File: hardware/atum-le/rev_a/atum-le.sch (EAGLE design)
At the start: 41 parts, among them J2 SH_MALE_2/1MM, J3 ATUM-HEADER, U1 CC2538, U2 FM25LBTDFN-8, U3 RV-3049-C3, U4 TPS62740, X1 EPSON-FA-128, X2 ABS05-32.768KHZ-T

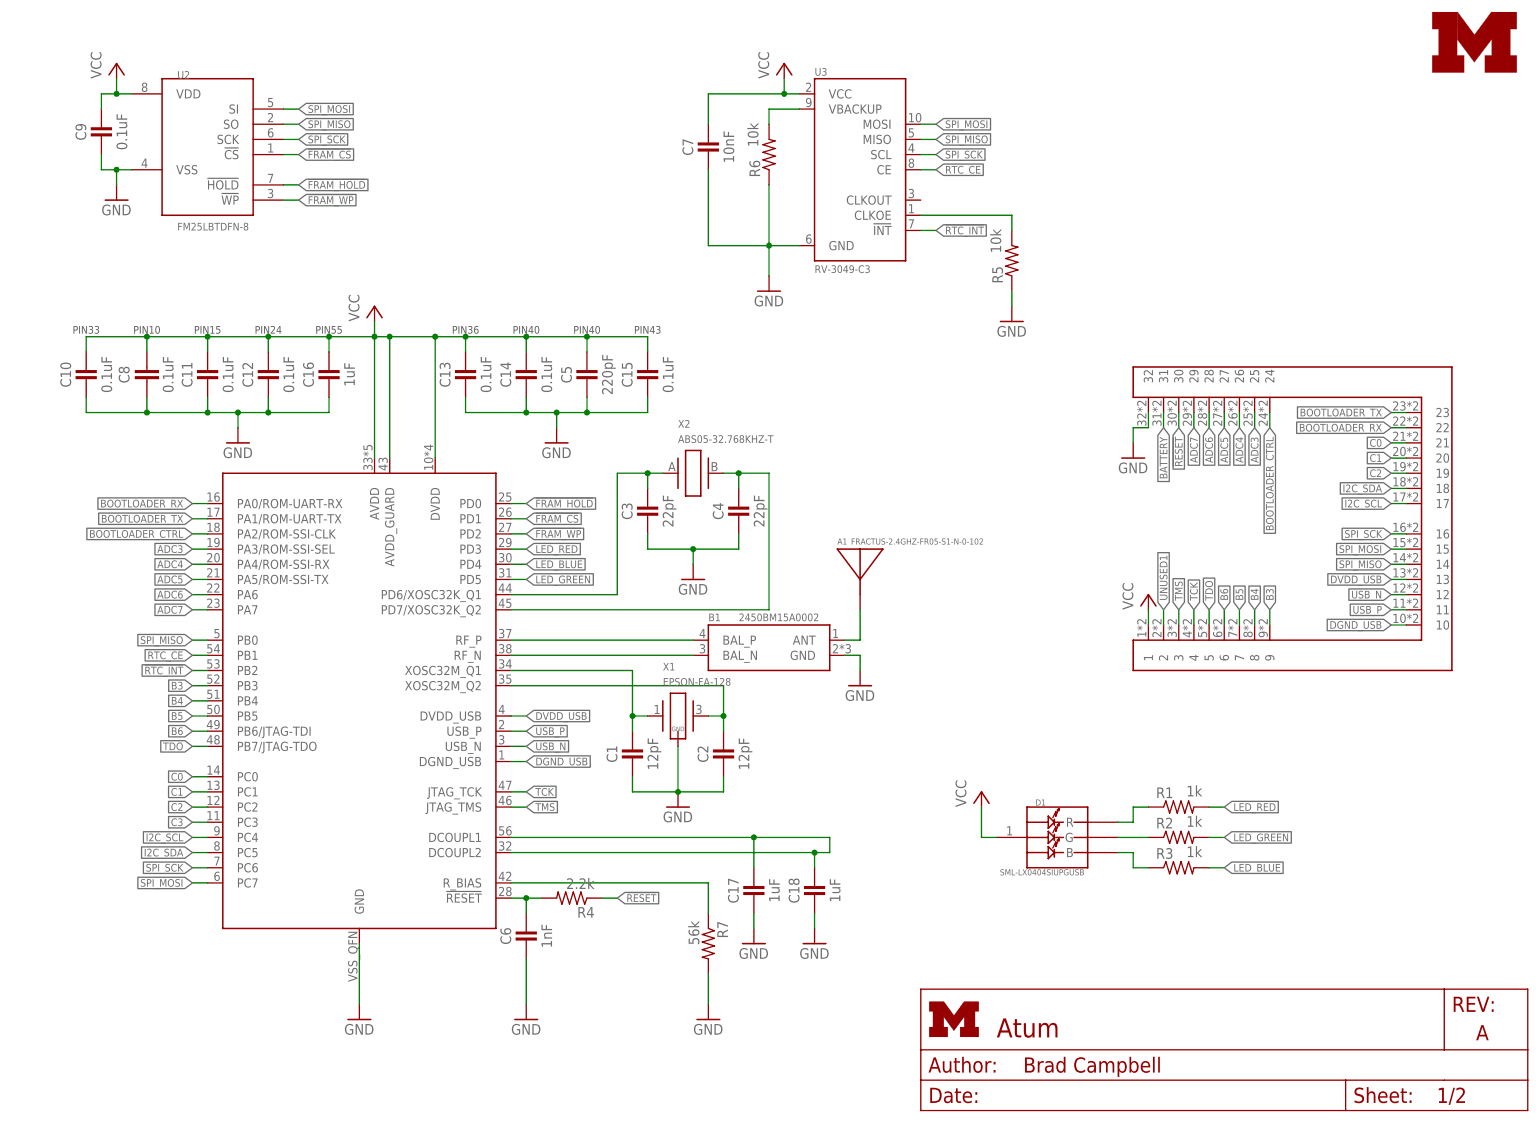
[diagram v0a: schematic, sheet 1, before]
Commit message: improved signal routing and mapping
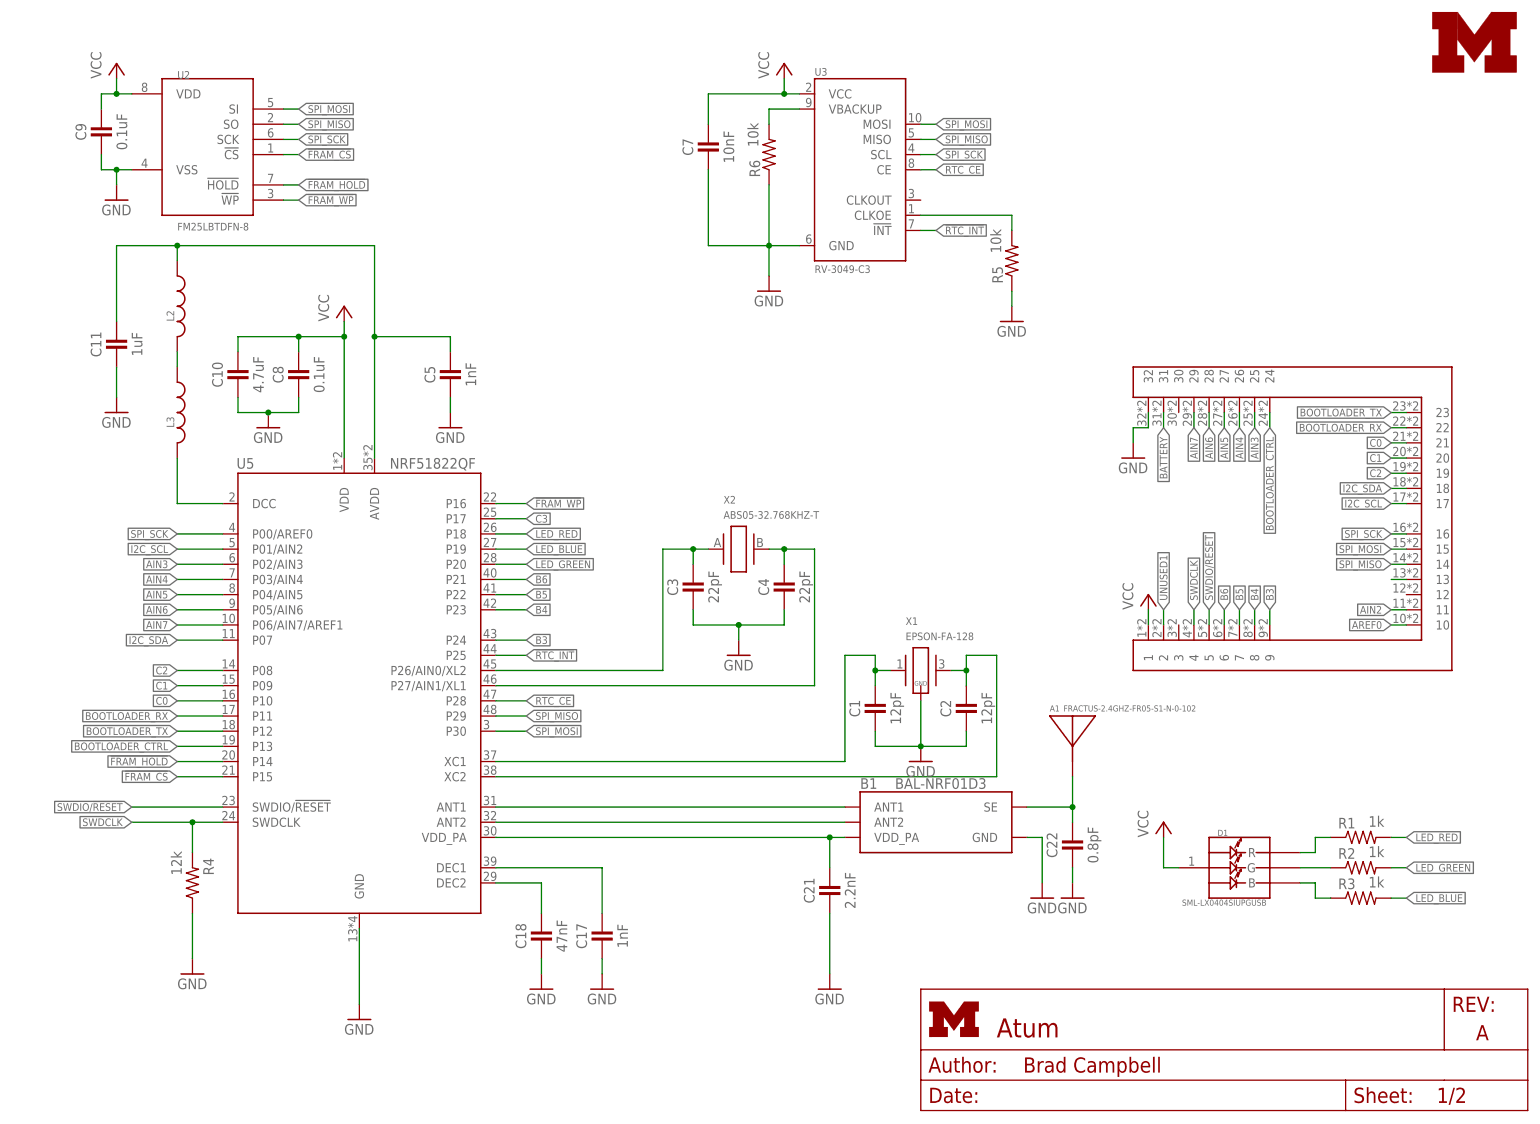
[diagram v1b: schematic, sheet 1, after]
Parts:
- removed C12, C13, C14, C15: 0.1uF, passives:CAPACITOR
- removed C16: 1uF, passives:CAPACITOR
- removed C6: 1nF, passives:CAPACITOR
- removed R7: 56k, passives:RESISTOR
- removed U1: CC2538, chips:CC2538
- added C21: 2.2nF, passives:CAPACITOR
- added C22: 0.8pF, passives:CAPACITOR
- added L2: (no value), passives:INDUCTOR0402
- added L3: (no value), passives:INDUCTOR0603
- added U5: NRF51822QF, chips:NRF51822QF
- B1: value 2450BM15A0002 -> BAL-NRF01D3; device chips:2450BM15A0002 -> chips:BAL-NRF01D3
- C10: value 0.1uF -> 4.7uF
- C11: value 0.1uF -> 1uF
- C17: value 1uF -> 1nF
- C18: value 1uF -> 47nF
- C5: value 220pF -> 1nF
- C8: device rcl:C-EUC0201 -> passives:CAPACITOR
- R4: value 2.2k -> 12k
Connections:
- removed net !RESET: J3.30, R4.1
- removed net ADC3: J3.25, U1.PA3/ROM-SSI-SEL
- removed net ADC4: J3.26, U1.PA4/ROM-SSI-RX
- removed net ADC5: J3.27, U1.PA5/ROM-SSI-TX
- removed net ADC6: J3.28, U1.PA6
- removed net ADC7: J3.29, U1.PA7
- removed net DGND_USB: J3.10, U1.DGND_USB
- removed net DVDD_USB: J3.13, U1.DVDD_USB
- removed net N$1: C6.1, R4.2, U1.!RESET
- removed net N$8: R7.1, U1.R_BIAS
- removed net RF_N: B1.BAL_N, U1.RF_N
- removed net RF_P: B1.BAL_P, U1.RF_P
- removed net TCK: J3.4, U1.JTAG_TCK
- removed net TDO: J3.5, U1.PB7/JTAG-TDO
- removed net TMS: J3.3, U1.JTAG_TMS
- removed net USB_N: J3.12, U1.USB_N
- removed net USB_P: J3.11, U1.USB_P
- new net AIN2: J3.11
- new net AIN3: J3.25, U5.P02/AIN3
- new net AIN4: J3.26, U5.P03/AIN4
- new net AIN5: J3.27, U5.P04/AIN5
- new net AIN6: J3.28, U5.P05/AIN6
- new net AIN7: J3.29, U5.P06/AIN7/AREF1
- new net AREF0: J3.10
- new net N$17: C17.1, U5.DEC1
- new net N$18: B1.ANT1, U5.ANT1
- new net N$19: B1.ANT2, U5.ANT2
- new net N$20: B1.VDD_PA, C21.1, U5.VDD_PA
- new net N$36: C11.1, C5.1, L2.1, U5.AVDD
- new net N$37: L2.2, L3.1
- new net N$38: L3.2, U5.DCC
- new net N$43: J3.13
- new net SWDCLK: J3.4, R4.2, U5.SWDCLK
- new net SWDIO/!RESET: J3.5, U5.SWDIO/!RESET
- net !FRAM_CS: now also U5.P15; no longer U1.PD1
- net !FRAM_HOLD: now also U5.P14; no longer U1.PD0
- net !FRAM_WP: now also U5.P16; no longer U1.PD2
- net !RTC_INT: now also U5.P25; no longer U1.PB2
- net ANTENNA: now also B1.SE, C22.1; no longer B1.ANT
- net B3: now also U5.P24; no longer U1.PB3
- net B4: now also U5.P23; no longer U1.PB4
- net B5: now also U5.P22; no longer U1.PB5
- net B6: now also U5.P21; no longer U1.PB6/JTAG-TDI
- net BOOTLOADER_CTRL: now also U5.P13; no longer U1.PA2/ROM-SSI-CLK
- net BOOTLOADER_RX: now also U5.P11; no longer U1.PA0/ROM-UART-RX
- net BOOTLOADER_TX: now also U5.P12; no longer U1.PA1/ROM-UART-TX
- net C0: now also U5.P10; no longer U1.PC0
- net C1: now also U5.P09; no longer U1.PC1
- net C2: now also U5.P08; no longer U1.PC2
- net C3: now also U5.P17; no longer U1.PC3
- net GND: now also C21.2, C22.2, R4.1; no longer C12.2, C13.2, C14.2, C15.2, C16.2, C6.2, R7.2, U1.GND
- net I2C_SCL: now also U5.P01/AIN2; no longer U1.PC4
- net I2C_SDA: now also U5.P07; no longer U1.PC5
- net LED_BLUE: now also U5.P19; no longer U1.PD4
- net LED_GREEN: now also U5.P20; no longer U1.PD5
- net LED_RED: now also U5.P18; no longer U1.PD3
- net N$10: now also U5.XC2; no longer U1.XOSC32M_Q2
- net N$13: now also U5.P27/AIN1/XL1; no longer U1.PD7/XOSC32K_Q2
- net N$15: now also U5.DEC2; no longer C17.1, U1.DCOUPL1, U1.DCOUPL2
- net N$6: now also U5.P26/AIN0/XL2; no longer U1.PD6/XOSC32K_Q1
- net N$9: now also U5.XC1; no longer U1.XOSC32M_Q1
- net RTC_CE: now also U5.P28; no longer U1.PB1
- net SPI_MISO: now also U5.P29; no longer U1.PB0
- net SPI_MOSI: now also U5.P30; no longer U1.PC7
- net SPI_SCK: now also U5.P00/AREF0; no longer U1.PC6
- net VCC: now also U5.VDD; no longer C11.1, C12.1, C13.1, C14.1, C15.1, C16.1, C5.1, U1.AVDD, U1.AVDD_GUARD, U1.DVDD
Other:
- note removed: "PIN10"
- note removed: "PIN15"
- note removed: "PIN24"
- note removed: "PIN33"
- note removed: "PIN36"
- note removed: "PIN40"
- note removed: "PIN43"
- note removed: "PIN55"
- moved on the sheet: A1, C1, C10, C11, C17, C18, C2, C3, C4, C5, D1, R1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

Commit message: finished up schematic and did more routing
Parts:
- removed R4: 12k, passives:RESISTOR
- removed R5, R6: 10k, passives:RESISTOR
- added R10, R8, R9: 1k, passives:RESISTOR0402_RES
- added U$1: RES_SWITCH, switches:RES_SWITCH
- R1, R2: value 1k -> 10k; device passives:RESISTOR -> passives:RESISTOR0402_RES
- R3: value 1k -> 12k; device passives:RESISTOR -> passives:RESISTOR0402_RES
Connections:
- net B3 renamed P24
- net B4 renamed P23
- net B5 renamed P22
- net B6 renamed P21
- net C0 renamed P10
- net C1 renamed P09
- net C2 renamed P08
- removed net AIN2: J3.11
- removed net AREF0: J3.10
- removed net C3: U5.P17
- removed net N$43: J3.13
- removed net UNUSED1: J3.2
- new net N$1: J3.30
- new net N$8: U$1.IN, U4.VSEL3, U4.VSEL4
- new net P17: J3.2, U5.P17
- net BATTERY: now also U$1.B; no longer U4.VSEL2, U4.VSEL4
- net GND: now also R1.2, R2.2, R3.1, U$1.A, U4.VSEL2; no longer R4.1, R5.1, R6.1, U4.VSEL3
- net LED_BLUE: now also R9.1; no longer R3.2
- net LED_GREEN: now also R10.1; no longer R2.2
- net LED_RED: now also R8.1; no longer R1.2
- net N$11: now also R10.2; no longer R2.1
- net N$12: now also R9.2; no longer R3.1
- net N$14: now also R2.1; no longer R6.2
- net N$16: now also R1.1; no longer R5.2
- net N$7: now also R8.2; no longer R1.1
- net SWDCLK: now also R3.2; no longer R4.2
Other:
- note added: "A-1.8V B-3.0V Output"
- note removed: "2.8V Output"
- moved on the sheet: C19, D1, R1, R2, R3

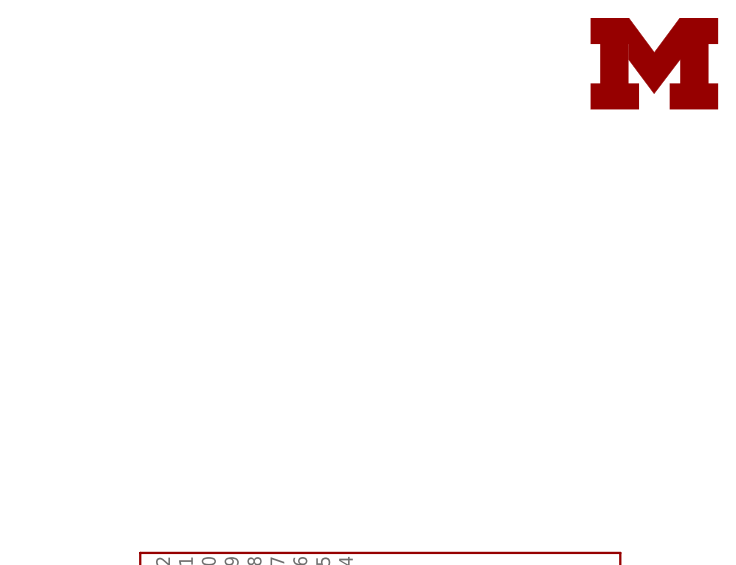
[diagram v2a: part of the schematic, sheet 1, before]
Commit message: added jtag, board routed but not DRCd
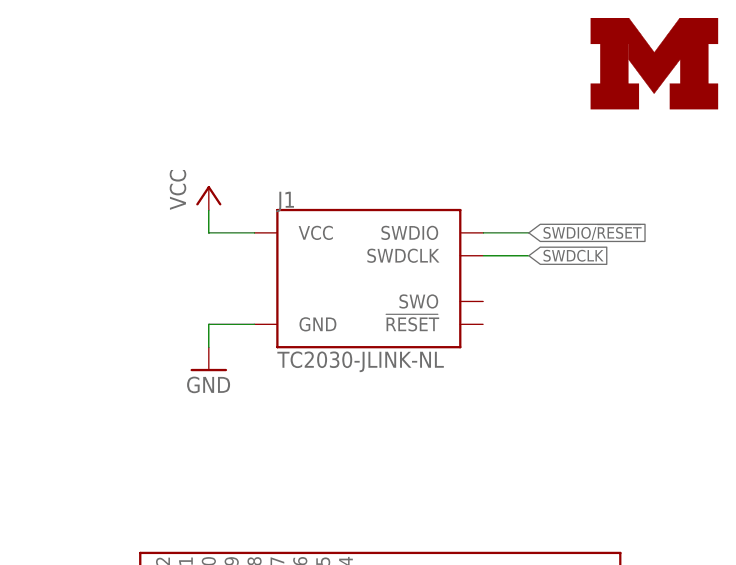
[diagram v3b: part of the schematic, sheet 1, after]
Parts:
- added J1: TC2030-JLINK-NL, connector:TC2030-JLINK-NL
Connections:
- net GND: now also J1.GND
- net SWDCLK: now also J1.SWDCLK
- net SWDIO/!RESET: now also J1.SWDIO
- net VCC: now also J1.VCC
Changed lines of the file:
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@@
 <part name="R1" library="passives" deviceset="RESISTOR" device="0402_RES" value="10k"/>
 <part name="R2" library="passives" deviceset="RESISTOR" device="0402_RES" value="10k"/>
+<part name="J1" library="connector" deviceset="TC2030-JLINK" device="-NL"/>
+<part name="P+4" library="supply1" deviceset="VCC" device=""/>
+<part name="GND5" library="supply1" deviceset="GND" device=""/>
 </parts>
 <sheets>
@@
 <attribute name="VALUE" x="118.618" y="163.83" size="1.778" layer="96" rot="R270"/>
 </instance>
+<instance part="J1" gate="G$1" x="208.28" y="154.94"/>
+<instance part="P+4" gate="VCC" x="190.5" y="165.1"/>
+<instance part="GND5" gate="1" x="190.5" y="144.78"/>
 </instances>
 <busses>
@@
 <wire x1="25.4" y1="25.4" x2="25.4" y2="33.02" width="0.1524" layer="91"/>
 <pinref part="R3" gate="G$1" pin="1"/>
+</segment>
+<segment>
+<pinref part="J1" gate="G$1" pin="GND"/>
+<pinref part="GND5" gate="1" pin="GND"/>
+<wire x1="195.58" y1="149.86" x2="190.5" y2="149.86" width="0.1524" layer="91"/>
+<wire x1="190.5" y1="149.86" x2="190.5" y2="147.32" width="0.1524" layer="91"/>
 </segment>
 </net>
@@
 <junction x="43.18" y="129.54"/>
 </segment>
+<segment>
+<pinref part="J1" gate="G$1" pin="VCC"/>
+<pinref part="P+4" gate="VCC" pin="VCC"/>
+<wire x1="195.58" y1="160.02" x2="190.5" y2="160.02" width="0.1524" layer="91"/>
+<wire x1="190.5" y1="160.02" x2="190.5" y2="162.56" width="0.1524" layer="91"/>
+</segment>
 </net>
 <net name="N$15" class="0">
@@
 <pinref part="R3" gate="G$1" pin="2"/>
 </segment>
+<segment>
+<pinref part="J1" gate="G$1" pin="SWDCLK"/>
+<wire x1="220.98" y1="157.48" x2="226.06" y2="157.48" width="0.1524" layer="91"/>
+<label x="226.06" y="157.48" size="1.27" layer="95" xref="yes"/>
+</segment>
 </net>
 <net name="SWDIO/!RESET" class="0">
@@
 <label x="15.24" y="50.8" size="1.27" layer="95" rot="R180" xref="yes"/>
 </segment>
-</net>
+<segment>
+<pinref part="J1" gate="G$1" pin="SWDIO"/>
+<wire x1="220.98" y1="160.02" x2="226.06" y2="160.02" width="0.1524" layer="91"/>
+<label x="226.06" y="160.02" size="1.27" layer="95" xref="yes"/>
+</segment>
+</net>

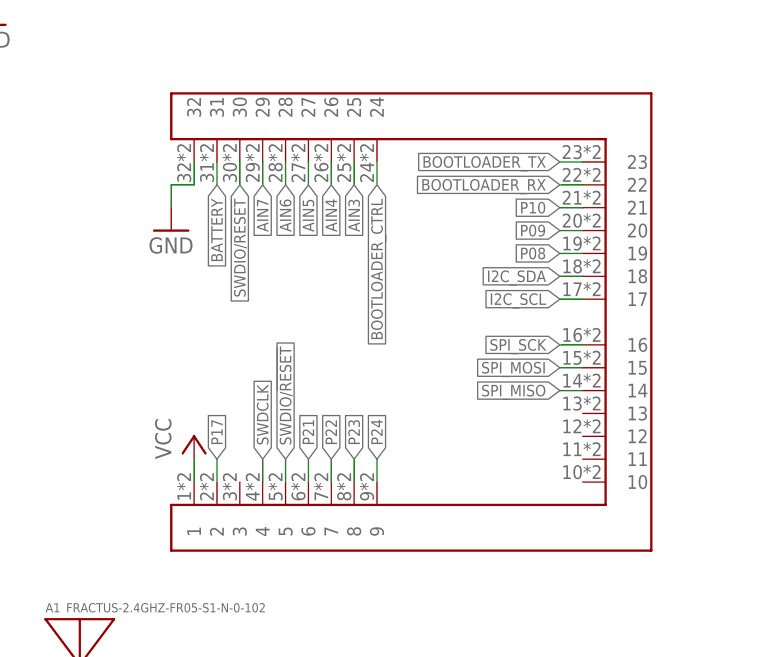
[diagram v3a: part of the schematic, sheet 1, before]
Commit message: fixed programming breakout, moved silk
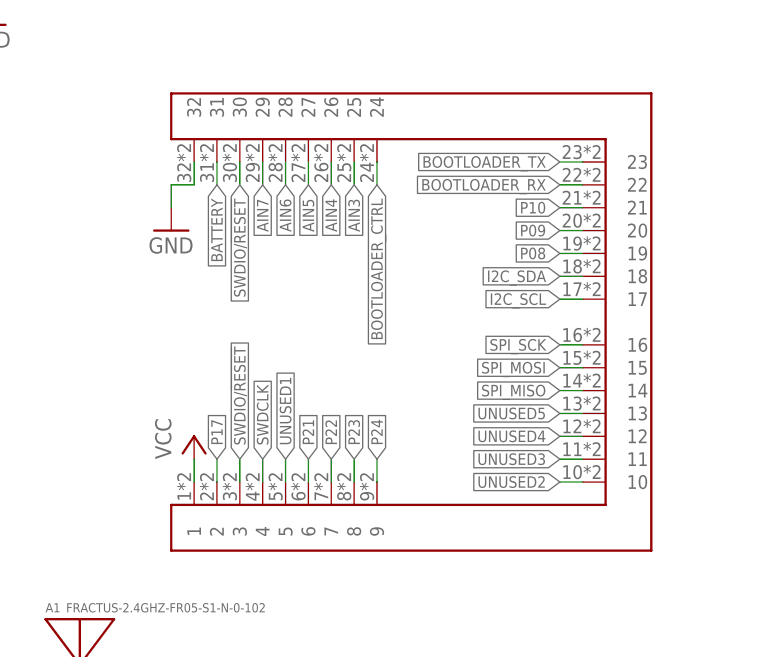
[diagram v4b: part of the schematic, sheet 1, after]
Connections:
- removed net N$1: J3.30
- new net UNUSED1: J3.5
- new net UNUSED2: J3.10
- new net UNUSED3: J3.11
- new net UNUSED4: J3.12
- new net UNUSED5: J3.13
- net SWDIO/!RESET: now also J3.3, J3.30; no longer J3.5
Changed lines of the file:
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@@
 <net name="SWDIO/!RESET" class="0">
-<segment>
-<wire x1="195.58" y1="83.82" x2="195.58" y2="81.28" width="0.1524" layer="91"/>
-<label x="195.58" y="83.82" size="1.27" layer="95" rot="R90" xref="yes"/>
-<pinref part="J3" gate="G$1" pin="5"/>
-<label x="190.5" y="114.3" size="1.27" layer="95" rot="R270" xref="yes"/>
-</segment>
 <segment>
 <pinref part="U5" gate="G$1" pin="SWDIO/!RESET"/>
@@
 <wire x1="220.98" y1="160.02" x2="226.06" y2="160.02" width="0.1524" layer="91"/>
 <label x="226.06" y="160.02" size="1.27" layer="95" xref="yes"/>
+</segment>
+<segment>
+<pinref part="J3" gate="G$1" pin="3"/>
+<wire x1="190.5" y1="81.28" x2="190.5" y2="83.82" width="0.1524" layer="91"/>
+<label x="190.5" y="83.82" size="1.27" layer="95" rot="R90" xref="yes"/>
+</segment>
+<segment>
+<pinref part="J3" gate="G$1" pin="30"/>
+<wire x1="190.5" y1="116.84" x2="190.5" y2="114.3" width="0.1524" layer="91"/>
+<label x="190.5" y="114.3" size="1.27" layer="95" rot="R270" xref="yes"/>
 </segment>
 </net>
@@
 </segment>
 </net>
-<net name="N$1" class="0">
-<segment>
-<pinref part="J3" gate="G$1" pin="30"/>
-<wire x1="190.5" y1="114.3" x2="190.5" y2="116.84" width="0.1524" layer="91"/>
-</segment>
-</net>
 <net name="P10" class="0">
 <segment>
@@
 </segment>
 </net>
+<net name="UNUSED1" class="0">
+<segment>
+<pinref part="J3" gate="G$1" pin="5"/>
+<wire x1="195.58" y1="81.28" x2="195.58" y2="83.82" width="0.1524" layer="91"/>
+<label x="195.58" y="83.82" size="1.27" layer="95" rot="R90" xref="yes"/>
+</segment>
+</net>
+<net name="UNUSED5" class="0">
+<segment>
+<pinref part="J3" gate="G$1" pin="13"/>
+<wire x1="228.6" y1="88.9" x2="226.06" y2="88.9" width="0.1524" layer="91"/>
+<label x="226.06" y="88.9" size="1.27" layer="95" rot="R180" xref="yes"/>
+</segment>
+</net>
+<net name="UNUSED4" class="0">
+<segment>
+<pinref part="J3" gate="G$1" pin="12"/>
+<wire x1="228.6" y1="86.36" x2="226.06" y2="86.36" width="0.1524" layer="91"/>
+<label x="226.06" y="86.36" size="1.27" layer="95" rot="R180" xref="yes"/>
+</segment>
+</net>
+<net name="UNUSED3" class="0">
+<segment>
+<pinref part="J3" gate="G$1" pin="11"/>
+<wire x1="228.6" y1="83.82" x2="226.06" y2="83.82" width="0.1524" layer="91"/>
+<label x="226.06" y="83.82" size="1.27" layer="95" rot="R180" xref="yes"/>
+</segment>
+</net>
+<net name="UNUSED2" class="0">
+<segment>
+<pinref part="J3" gate="G$1" pin="10"/>
+<wire x1="228.6" y1="81.28" x2="226.06" y2="81.28" width="0.1524" layer="91"/>
+<label x="226.06" y="81.28" size="1.27" layer="95" rot="R180" xref="yes"/>
+</segment>
+</net>
